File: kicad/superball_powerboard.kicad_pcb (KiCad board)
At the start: 4 copper layers, 100 x 50 mm, 146 parts, among them J1 MICROCLASP_HDRX3, J2 MICROCLASP_HDRX3, J3 MICROCLASP_HDRX2, J4 MICROCLASP_HDRX2, J5 MICROCLASP_HDRX2, J6 MICROCLASP_HDRX2, J7 MICROCLASP_HDRX2, J8 MICROCLASP_HDRX2, J9 MICROCLASP_HDRX2, Q1 MCP73832, Q10 FDS6898AZ, Q11 FDS6898AZ, Q12 LTC1982, Q13 LTC1982, Q14 FDS6898AZ, Q15 FDS6898AZ, Q16 RF803D, Q17 PSMN013-80YS, Q2 LM3478, Q3 TPS54540, Q4 LT1910, Q5 0S102011MA1QN1, Q6 PSMN013-80YS, Q7 PSMN013-80YS, Q8 LTC1982, Q9 ACS711KLCTR-12AB-T, U1 SI1970DH, U3 SN65HVD232, U4 DSPIC33E128MC506, U5 MCP1700

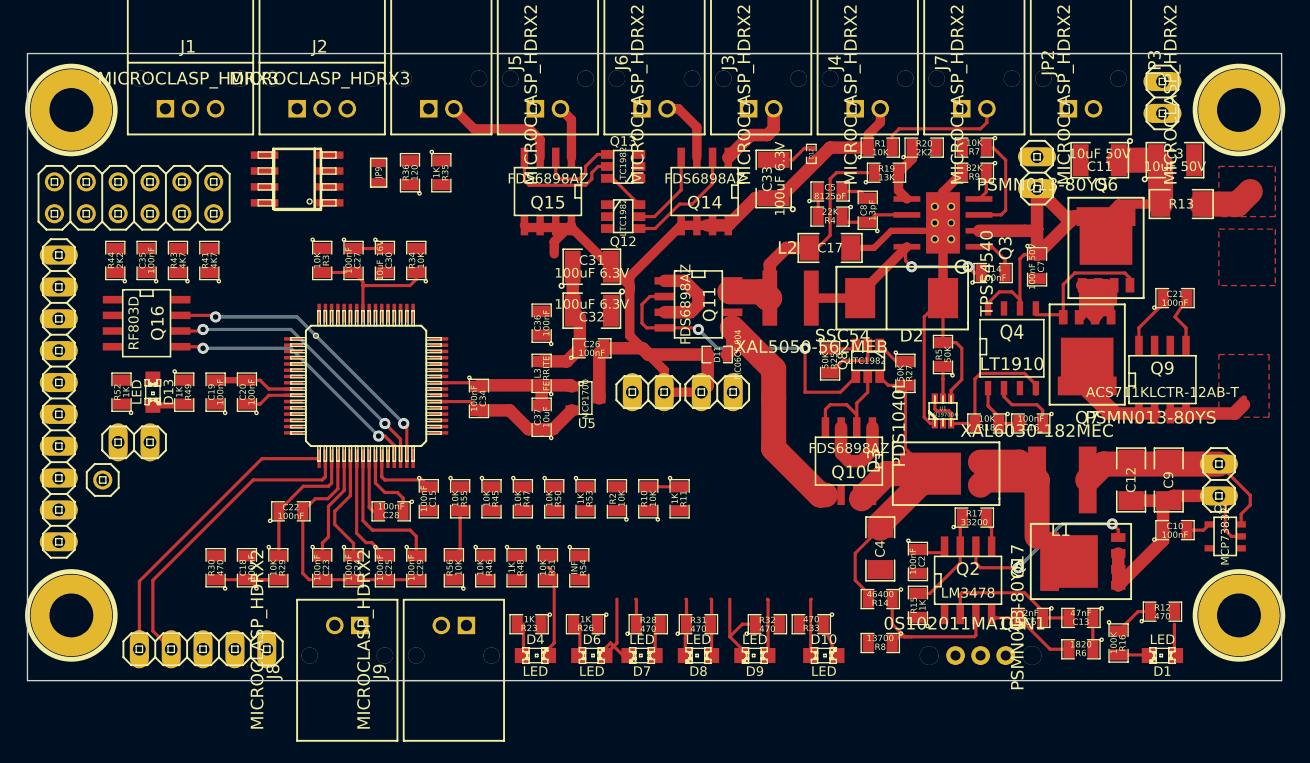
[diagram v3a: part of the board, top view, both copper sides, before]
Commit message: finished routing (preliminary). Added a current sensor for the 5.5V line.
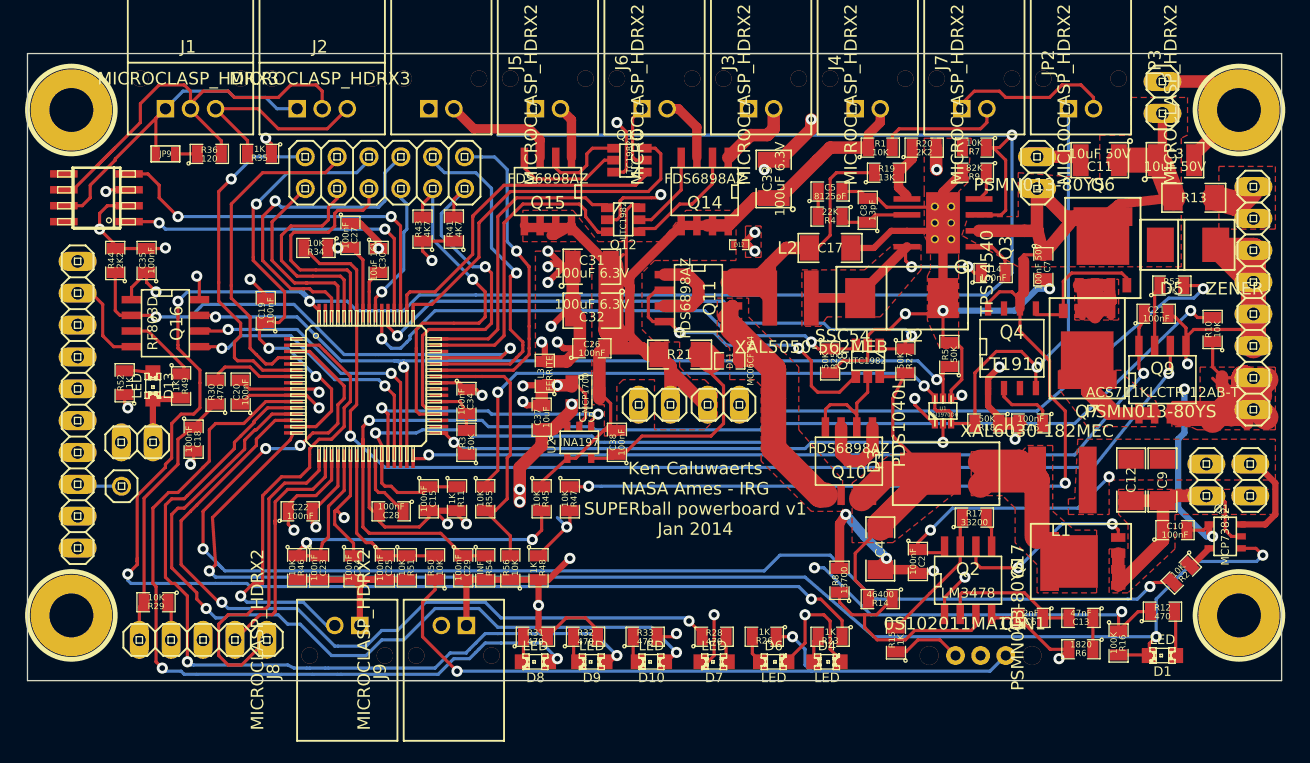
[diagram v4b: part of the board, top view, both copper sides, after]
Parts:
- removed C36: 100nF, SM0805
- added C38: 100nF, SM0805, F.Cu at (67.0, 51.0)
- added D5: ZENER, 403A-03, F.Cu at (114.8, 35.2)
- added JP13: PINHD-1X8, pinhead-1X08, F.Cu at (117.8, 39.5)
- added JP14: PINHD-1X2, pinhead-1X02, F.Cu at (117.5, 54.0)
- added R21: 0.02, SM1206, F.Cu at (72.0, 44.0)
- added U2: INA197, SOT23-5, F.Cu at (64.0, 51.0)
- R18, R3: value 10K -> 50K
- moved R53 49.7 mm to (111.2, 38.5), turned to 0 degrees
- moved R10 47.0 mm to (114.5, 42.0)
- moved R2 45.4 mm to (112.0, 61.5), turned to 225 degrees
- moved R23 24.0 mm to (84.0, 66.5)
- moved D4 23.3 mm to (83.8, 68.5)
- moved JP4 20.1 mm to (48.5, 29.5)
- moved R41 19.7 mm to (54.0, 34.0)
- moved R43 19.7 mm to (51.5, 34.0)
- moved R3 18.5 mm to (55.0, 51.0), turned to 90 degrees
- moved R11 17.8 mm to (54.2, 55.5)
- moved JP9 17.1 mm to (31.0, 28.0), turned to 0 degrees
- moved R36 16.1 mm to (34.5, 28.0), turned to 0 degrees
- moved U3 16.1 mm to (25.5, 31.5)
- moved R46 15.0 mm to (41.5, 61.0)
- moved R35 14.6 mm to (38.5, 28.0), turned to 180 degrees
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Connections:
- net N-0000042 renamed /VBAT_HF_SW
- net N-0000044 renamed /VBAT_SW
- net N-0000066 renamed /5V5_MERGE
- C19 pad 1: /EX_9 -> /EX_4
- D11 pad 2: /5V5 -> /5V5_FUSE
- D3 pad 1: N-0000055 (its old number) -> /VBACKUP_SW
- JP6 pad 2: /VBAT_IN -> /VBAT
- L1 pad 1: N-0000055 (its old number) -> /VBACKUP_SW
- Q17 pad 5: N-0000055 (its old number) -> /VBACKUP_SW
- R41 pad 1: N-0000063 (its old number) -> 3V3
- R43 pad 1: N-0000063 (its old number) -> 3V3
- U4 pad 1: /G_BAT_PIC -> N-00000126
- U4 pad 15: /EX_9 -> /EX_4
- U4 pad 32: /EX_8 -> /EN_MOTOR_CURRENT
- U4 pad 33: N-00000111 -> /G_BAT_PIC
- U4 pad 4: /EX_1 -> /EX_5
- U4 pad 43: /EX_7 -> /EX_1
- U4 pad 44: /EX_6 -> /EX_2
- U4 pad 47: /EN_OUT_4 -> /EN_OUT_2
- U4 pad 48: /EN_OUT_3 -> /EN_OUT_1
- U4 pad 49: /EN_OUT_2 -> /EN_OUT_4
- U4 pad 50: /EN_OUT_1 -> /EN_OUT_3
- U4 pad 55: N-0000099 -> /EX_7
- U4 pad 59: /EN_MOTOR_CURRENT -> /EX_8
- U4 pad 6: /EX_2 -> /EX_6
- U4 pad 60: /EX_4 -> /EX_9
- U4 pad 61: /EX_3 -> /EX_10
- U4 pad 62: /EX_10 -> /EX_3
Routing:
- net /VBAT_5V5_EN: track 8.24 -> 220.1 mm, vias 0 -> 5
- net GND: track 162.9 -> 358.2 mm, vias 0 -> 45
- net /VBACKUP_STAT: track 2.47 -> 110.4 mm, vias 0 -> 3
- net /VBACKUP_CHARGE_EN: track 0.00 -> 106.3 mm, vias 0 -> 4
- net /MOTOR_CURRENT_FLT: track 0.00 -> 90.5 mm, vias 0 -> 2
- net /AN11: track 11.3 -> 94.5 mm, vias 0 -> 2
- net /5V5: track 76.8 -> 151.7 mm, vias 0 -> 3
- net /VMOTOR_V: track 8.03 -> 82.8 mm, vias 0 -> 2
- net /VMOTOR_EN: track 14.8 -> 82.9 mm, vias 0 -> 3
- net /VBAT: track 49.2 -> 116.4 mm, vias 0 -> 2
- net /EN_MOTOR_CURRENT: track 4.60 -> 66.4 mm, vias 0 -> 2
- net /B_LED: track 4.52 -> 65.6 mm, vias 0 -> 2
- net /STATUS_LED: track 2.02 -> 63.0 mm, vias 0 -> 2
- net /G_LED: track 4.52 -> 64.6 mm, vias 0 -> 2
- net /R_LED: track 4.52 -> 63.3 mm, vias 0 -> 2
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- added copper zone on F.Cu, net /5V5
- added copper zone on Inner2.Cu, net /5V5
- added copper zone on F.Cu, net /5V5_MERGE
- added copper zone on F.Cu, net /5V5_VBACKUP
- added copper zone on F.Cu, net /5V5_VBAT
- added copper zone on F.Cu, net /VBACKUP
- added copper zone on Inner2.Cu, net /VBACKUP
- added copper zone on F.Cu, net /VBACKUP_SW
- added copper zone on F.Cu, net /VBAT
- added copper zone on Inner2.Cu, net /VBAT
- added copper zone on F.Cu, net /VBAT_HF_SW
- added copper zone on F.Cu, net /VBAT_SW
- added copper zone on F.Cu, net /VBAT_SWITCHED
- added copper zone on Inner2.Cu, net 3V3
- added copper zone on Inner1.Cu, net GND
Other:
- board text added: "Ken Caluwaerts NASA Ames - IRG SUPERball powerboard v1 Jan 2014"

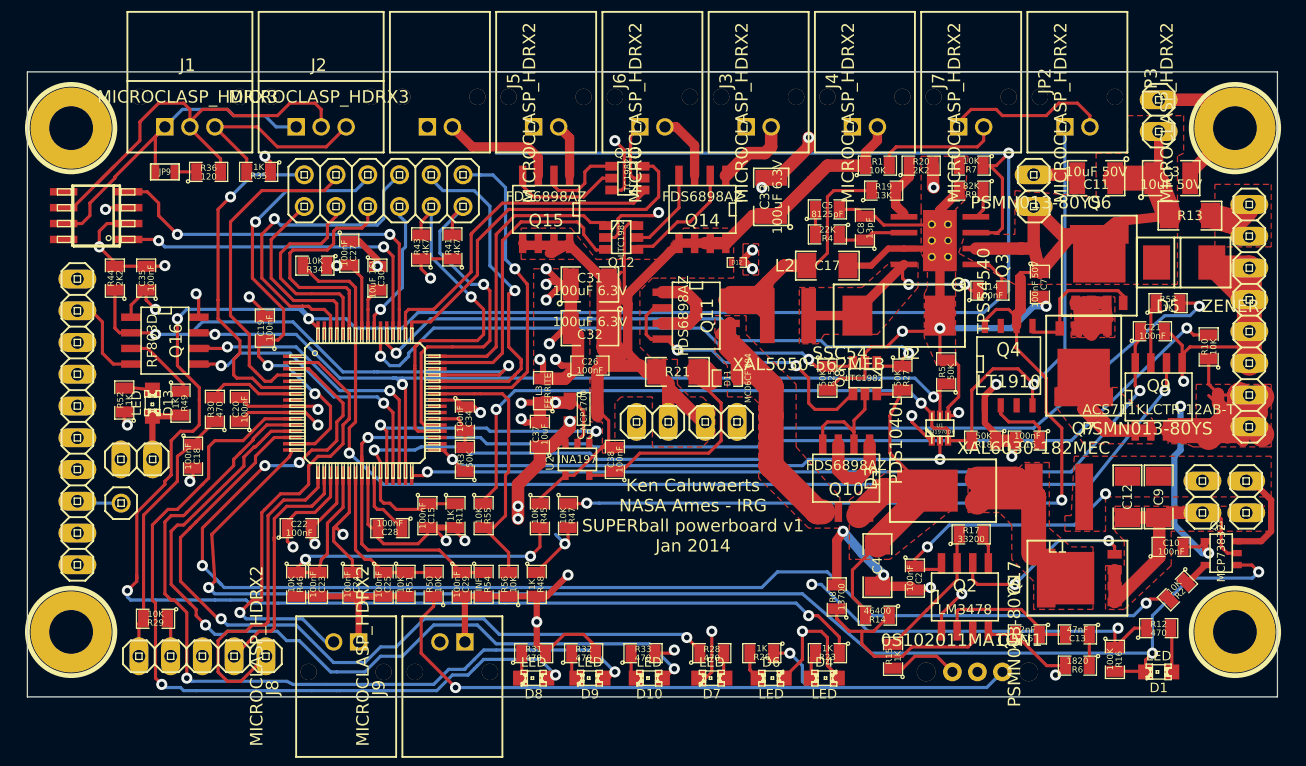
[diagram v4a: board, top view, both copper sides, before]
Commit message: cleaned up traces, added test pins etc
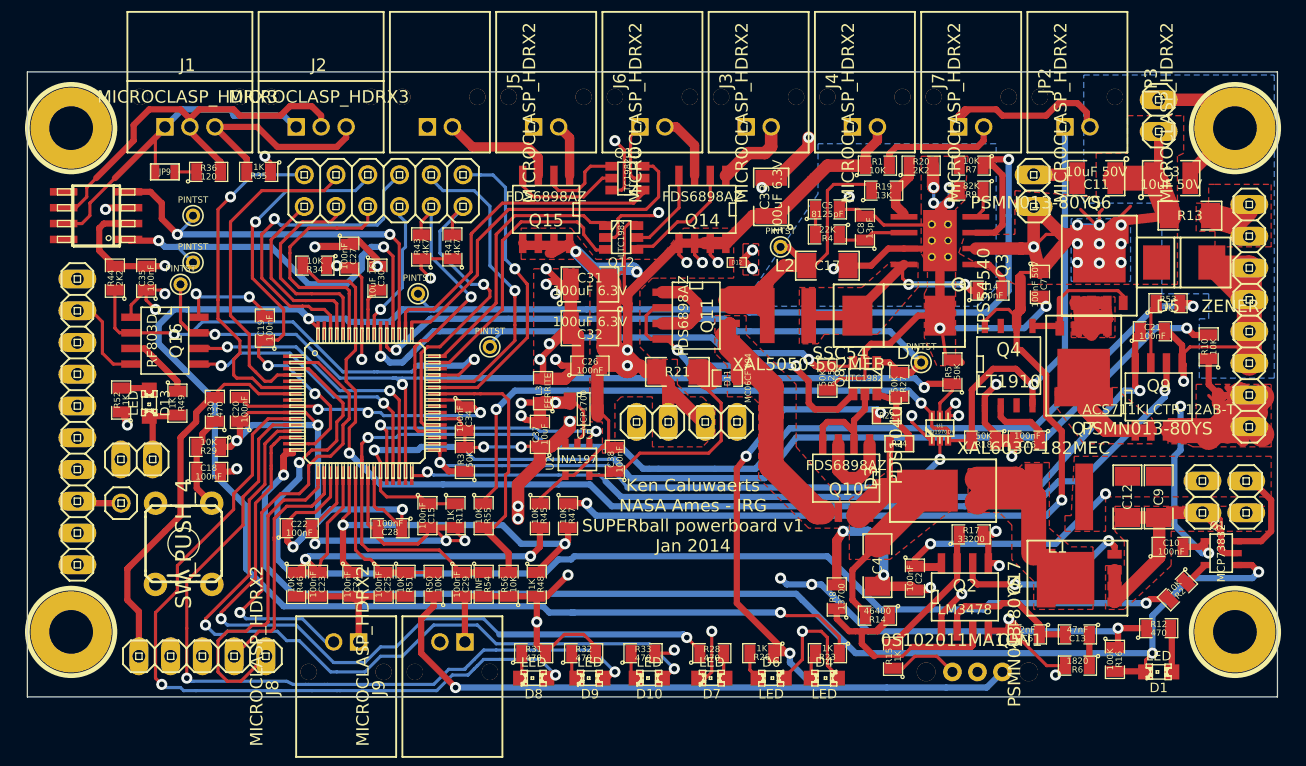
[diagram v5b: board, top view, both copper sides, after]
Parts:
- added PINTST: Val*, PINTST, F.Cu at (33.2, 31.5)
- added PINTST: Val*, PINTST, F.Cu at (33.2, 35.2)
- added PINTST: Val*, PINTST, F.Cu at (32.2, 37.0)
- added PINTST: Val*, PINTST, F.Cu at (57.0, 42.0)
- added PINTST: Val*, PINTST, F.Cu at (51.2, 37.8)
- added PINTST: Val*, PINTST, F.Cu at (80.2, 34.0)
- added PINTST: Val*, PINTST, F.Cu at (91.5, 43.2)
- added R22: 0, SM0603, F.Cu at (88.8, 47.5)
- added R24: INF, SM0603, F.Cu at (89.8, 49.8)
- added SW1: SW_PUSH_4, ASL-B3F-1020, F.Cu at (32.5, 57.8)
- moved R29 14.4 mm to (34.5, 50.0)
- moved C18 1.77 mm to (34.5, 52.0), turned to 0 degrees
- moved R27 0.56 mm to (89.8, 45.0)
- moved R5 0.50 mm to (94.0, 44.0)
- moved C27 0.25 mm to (45.8, 34.8)
- moved D13 0.25 mm to (29.8, 46.5)
- moved R49 0.25 mm to (32.0, 46.5)
- moved R52 0.25 mm to (27.5, 46.2)
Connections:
- net N-0000055 renamed /5V_CUR
- C18 pad 1: /MCLR -> N-00000123
- Q8 pad 6: /5V5_VBACKUP -> N-0000050
- R27 pad 2: /5V5_VBACKUP -> N-0000050
- R29 pad 2: /MCLR -> N-00000123
- R30 pad 1: /MCLR -> N-00000123
- R30 pad 2: N-0000063 (its old number) -> /MCLR
- U4 pad 7: N-0000063 (its old number) -> /MCLR
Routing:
- net 3V3: track 92.8 -> 171.8 mm, vias 12 -> 19
- net /SWITCH_ON: track 58.2 -> 136.6 mm, vias 2 -> 4
- net GND: track 358.2 -> 432.5 mm, vias 45 -> 54
- net /VMOTOR_EN: track 82.9 -> 140.6 mm
- net /VBAT_5V5_EN: track 220.1 -> 181.6 mm, vias 5 -> 3
- net /VBAT: track 116.4 -> 154.4 mm, vias 2 -> 12
- net /VBACKUP_STAT: track 110.4 -> 142.1 mm
- net /CAN_TX: track 27.7 -> 52.8 mm
- net /EN_VBACKUP_5V5: track 48.9 -> 72.5 mm, vias 2 -> 1
- net /AN7: track 15.6 -> 36.7 mm
- net /5V5: track 151.7 -> 171.2 mm, vias 3 -> 10
- net /STATUS_LED: track 63.0 -> 74.6 mm
- net /VMOTOR: track 51.0 -> 62.3 mm
- net N-0000047: track 13.2 -> 24.5 mm, vias 0 -> 1
- net /VBACKUP_CHARGE_EN: track 106.3 -> 96.0 mm, vias 4 -> 2
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- added copper zone on B.Cu, net /VBAT
- added copper zone on B.Cu, net GND

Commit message: silkscreen layout
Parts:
- removed JP12: PINHD-1X2, pinhead-1X02
- removed PINTST (x2): Val*, PINTST
- added CAN_RX: Val*, PINTST, F.Cu at (33.2, 31.5)
- added LEARN: PINHD-1X2, pinhead-1X02, F.Cu at (28.8, 51.0)
- added VBAT_5V5_EN: Val*, PINTST, F.Cu at (51.2, 37.8)
- RF RECEIVER: renamed from JP10
- renumbered PINTST to 5V5_VBAT, JP7 to ?, JP8 to ?, JP13 to ?, JP11 to ANT, PINTST to CAN_TX, PINTST to EN_VBACKUP_5V5, PINTST to EN_VBAT_5V5, JP14 to GND, PINTST to G_BAT_KILL, JP5 to VBACKUP
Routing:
- net 3V3: track 171.8 -> 181.2 mm
- net /VMOTOR: track 62.3 -> 70.1 mm
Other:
- board text added: "1"
- board text added: "10"
- board text added: "3V3"
- board text added: "3V3 OUT"
- board text added: "5V5"
- board text added: "5V5 OUT"
- board text added: "5V5 SW1"
- board text added: "5V5 SW2"
- board text added: "5V5 SW3"
- board text added: "5V5 SW4"
- board text added: "B"
- board text added: "BUZZER"
- board text added: "CAN"
- board text added: "EX1"
- board text added: "EX10"
- board text added: "EX2"
- board text added: "EX3"
- board text added: "EX4"
- board text added: "EX5"
- board text added: "EX6"
- board text added: "EX7"
- board text added: "EX8"
- board text added: "EX9"
- board text added: "G"
- board text added: "GND"
- board text added: "H"
- board text added: "KILL"
- board text added: "L"
- board text added: "MCLR(1)"
- board text added: "OFF"
- board text added: "ON"
- board text added: "PGEC"
- board text added: "PGED"
- board text added: "R"
- board text added: "RESET"
- board text added: "SCL"
- board text added: "SDA"
- board text added: "STATUS"
- board text added: "SUPERball powerboard v1 Ken Caluwaerts NASA Ames - IRG Jan 2014"
- board text added: "SWITCH ON"
- board text added: "VBACKUP"
- board text added: "VBACKUP STATUS"
- board text added: "VBAT"
- board text added: "VBAT_5V5_EN"
- board text added: "VBAT_IN"
- board text added: "VMOTOR"
- board text added: "powerboard v1 NASA ARC IRG Ken Caluwaerts"
- board text removed: "Ken Caluwaerts NASA Ames - IRG SUPERball powerboard v1 Jan 2014"
